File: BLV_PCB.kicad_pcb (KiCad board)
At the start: 4 copper layers, 89.7 x 89.7 mm, 88 parts, among them J1 Cube0 JST-PH, J2 Cube0 JST-PH, J3 Cube0 JST-PH, J4 Micro_SD_Card, J5 Dupont Debug Headers, J6 USB_C_USB2.0_16P, J8 USB_C_USB2.0_16P, Q1 Si2301CDS, SW1 SW_Push, SW2 SW_Push, SW5 SW_Push, U1 W25Q128JVS, U2 RP2350_60QFN, U3 TP4056, U4 AMS1117-3.3, U5 TPS61230DRCR, U6 NEO-M9N, U9 E22-400M33S, Y1 ABM8_262_T3

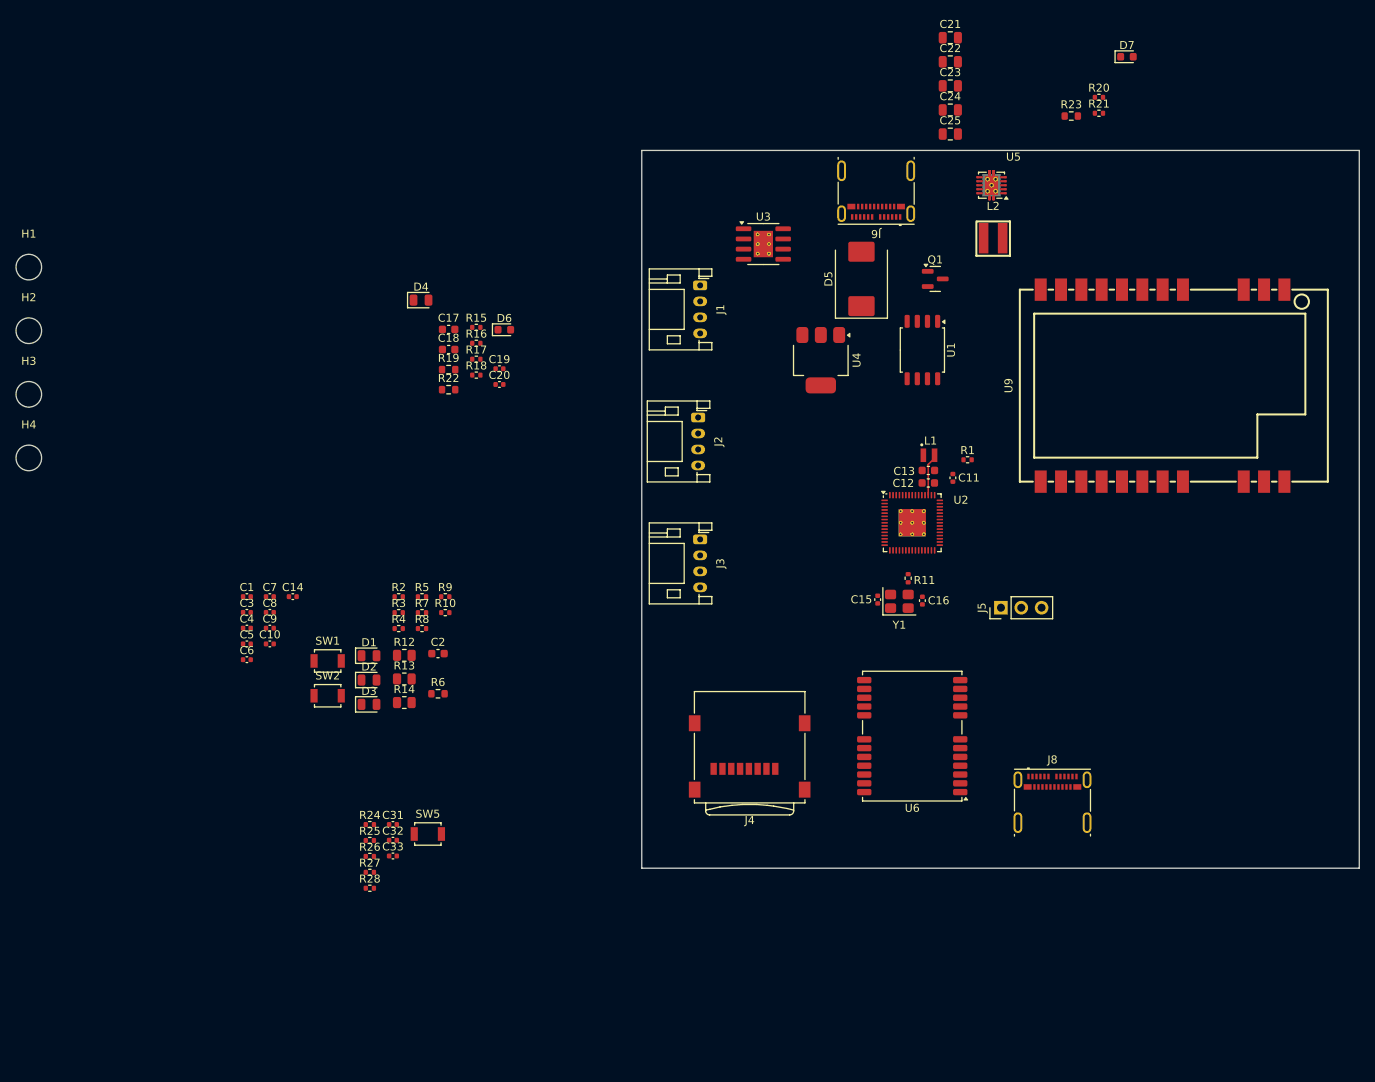
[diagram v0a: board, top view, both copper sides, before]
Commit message: Added footprints & routing 30%
- Added Dupont debug headers for UARTs.
- Added footprints: 18650 battery, E32-400M30S.
- Remove Battery Charger due to reliability issue.
- Routing 5V SMPS, 3V3 Regulator, Battery Holder.
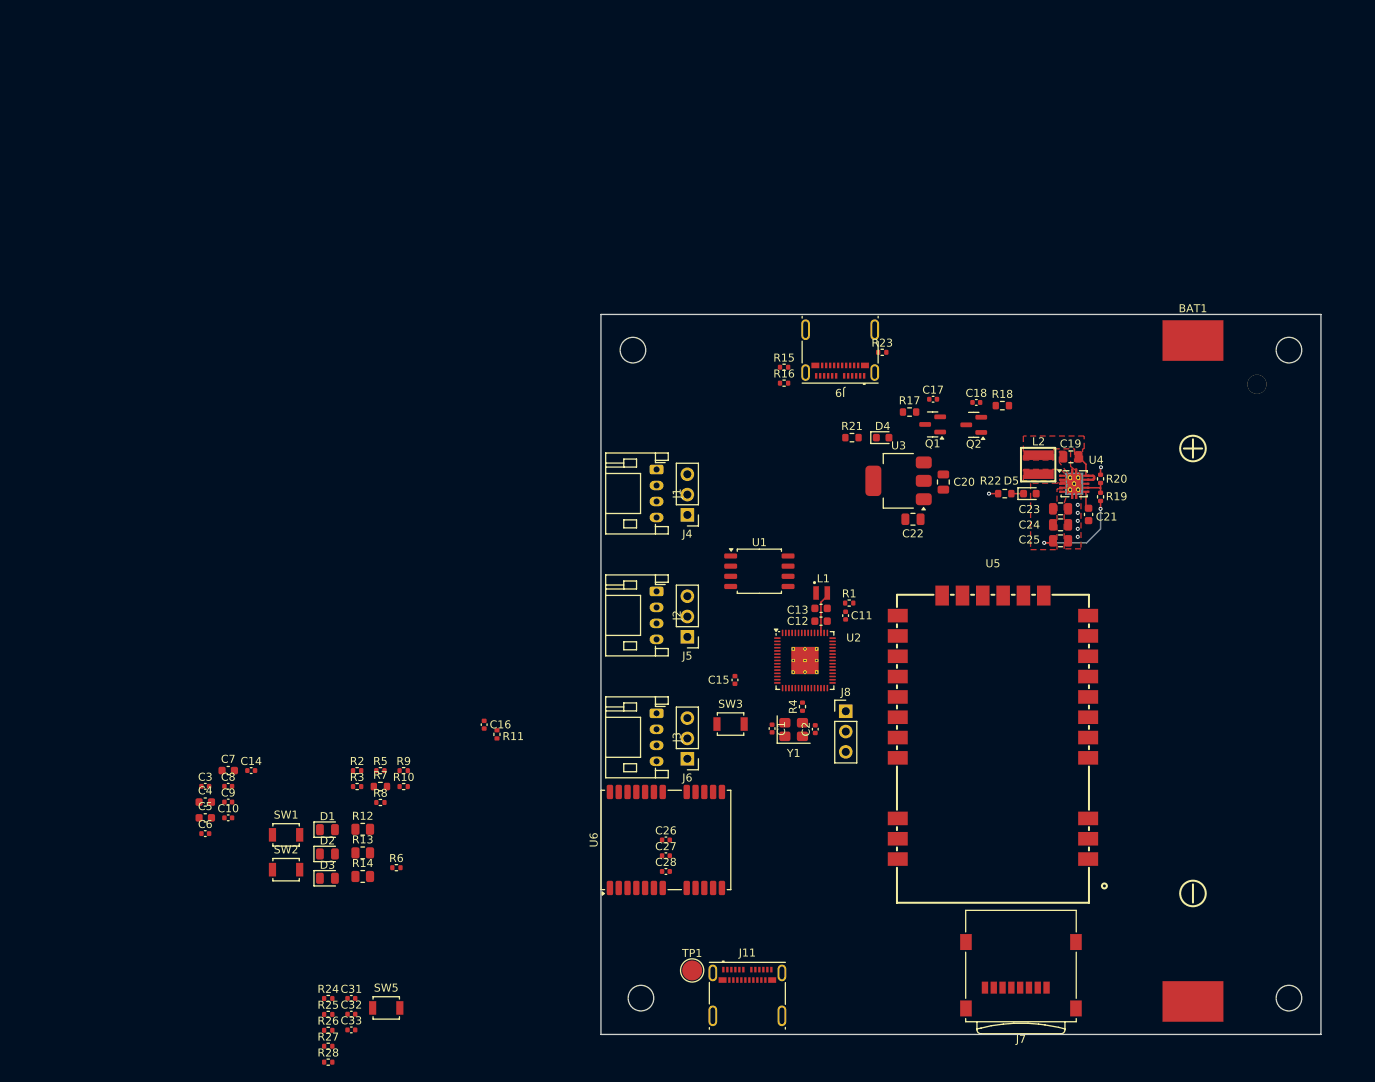
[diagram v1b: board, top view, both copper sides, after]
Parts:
- removed D6: YELLOW, LED_SMD:LED_0603_1608Metric
- removed D7: GREEN, LED_SMD:LED_0603_1608Metric
- removed U9: E22-400M33S, WIRELM-SMD_E22-400M30S:WIRELM-SMD_E22-400M33S
- added BAT1: BH-18650-B6AA002, easyeda2kicad:BATTERY-SMD_18650-1S-L77.1-W20.7-1, F.Cu at (204.0, 84.6)
- added C26: 10uF, Capacitor_SMD:C_0402_1005Metric, F.Cu at (138.1, 105.7)
- added C27: 1uF, Capacitor_SMD:C_0402_1005Metric, F.Cu at (138.1, 107.7)
- added C28: 100nF, Capacitor_SMD:C_0402_1005Metric, F.Cu at (138.1, 109.6)
- added J11: USB_C_USB2.0_16P, Connector_USB:USB_C_Receptacle_Molex_105450-0101, F.Cu at (148.3, 125.1)
- added J7: Micro_SD_Card, Connector_Card:microSD_HC_Wuerth_693072010801, F.Cu at (182.5, 122.6)
- added J9: USB_C_USB2.0_16P, Connector_USB:USB_C_Receptacle_Molex_105450-0101, F.Cu at (159.9, 44.5)
- added Q2: Si2301CDS, Package_TO_SOT_SMD:SOT-23, F.Cu at (176.6, 53.8)
- added SW3: SW_Push, Button_Switch_SMD:SW_SPST_B3U-1000P, F.Cu at (146.2, 91.2)
- added TP1: TestPoint, TestPoint:TestPoint_Pad_D2.5mm, F.Cu at (141.4, 122.0)
- C1: value 100n -> 15p
- C11, C12, C13: value 4u7 -> 100n
- C15, C16: value 15p -> 100n
- C17, C18: value 10u -> 100n; footprint Capacitor_SMD:C_0603_1608Metric -> Capacitor_SMD:C_0402_1005Metric
- C19: value 10u -> 22u; footprint Capacitor_SMD:C_0402_1005Metric -> Capacitor_SMD:C_0805_2012Metric
- C2: value 4u7 -> 15p; footprint Capacitor_SMD:C_0603_1608Metric -> Capacitor_SMD:C_0402_1005Metric
- C20: footprint Capacitor_SMD:C_0402_1005Metric -> Capacitor_SMD:C_0805_2012Metric
- C21: value 22u -> 10u; footprint Capacitor_SMD:C_0805_2012Metric -> Capacitor_SMD:C_0603_1608Metric
- C4, C5, C7: value 100n -> 4u7; footprint Capacitor_SMD:C_0402_1005Metric -> Capacitor_SMD:C_0603_1608Metric
- C8: value 100n -> 4u7
- D4: footprint LED_SMD:LED_0805_2012Metric -> LED_SMD:LED_0603_1608Metric
- D5: value SS36-E3/57T -> GREEN; footprint Diode_SMD:D_SMC -> LED_SMD:LED_0603_1608Metric
- J1, J2, J3: value Cube0 JST-PH -> Cube0_UART_JST-PH
- J4: value Micro_SD_Card -> Cube0_UART_Debug; footprint Connector_Card:microSD_HC_Wuerth_693072010801 -> Connector_PinHeader_2.54mm:PinHeader_1x03_P2.54mm_Vertical
- J5: value Dupont Debug Headers -> Cube0_UART_Debug
- J6: value USB_C_USB2.0_16P -> Cube0_UART_Debug; footprint Connector_USB:USB_C_Receptacle_Molex_105450-0101 -> Connector_PinHeader_2.54mm:PinHeader_1x03_P2.54mm_Vertical
- J8: value USB_C_USB2.0_16P -> Dupont Debug Headers; footprint Connector_USB:USB_C_Receptacle_Molex_105450-0101 -> Connector_PinHeader_2.54mm:PinHeader_1x03_P2.54mm_Vertical
- R1: value 33 -> DNF
- R11: value 1k -> 10k
- R17: value 5K1 -> 100k; footprint Resistor_SMD:R_0402_1005Metric -> Resistor_SMD:R_0603_1608Metric
- R18: value 2k2 -> 100k; footprint Resistor_SMD:R_0402_1005Metric -> Resistor_SMD:R_0603_1608Metric
- R19: value 10k -> 200k; footprint Resistor_SMD:R_0603_1608Metric -> Resistor_SMD:R_0402_1005Metric
- R2: value 27 -> 0
- R20: value 200k -> 49k9
- R21: value 49k9 -> 2k2; footprint Resistor_SMD:R_0402_1005Metric -> Resistor_SMD:R_0603_1608Metric
- R23: value 2k2 -> 5k1; footprint Resistor_SMD:R_0603_1608Metric -> Resistor_SMD:R_0402_1005Metric
- R25: value 5k1 -> 10k
- R3: value 27 -> 10k
- R4: value 10k -> 1k
- R5: value DNF -> 10k
- R6: value 1k -> 33; footprint Resistor_SMD:R_0603_1608Metric -> Resistor_SMD:R_0402_1005Metric
- R7: value 0 -> 1k; footprint Resistor_SMD:R_0402_1005Metric -> Resistor_SMD:R_0603_1608Metric
- R8, R9: value 10k -> 27
- U3: value TP4056 -> AMS1117-3.3; footprint Package_SO:SOIC-8-1EP_3.9x4.9mm_P1.27mm_EP2.41x3.3mm_ThermalVias -> Package_TO_SOT_SMD:SOT-223-3_TabPin2
- U4: value AMS1117-3.3 -> TPS61230DRCR; footprint Package_TO_SOT_SMD:SOT-223-3_TabPin2 -> Package_SON:Texas_S-PVSON-N10_ThermalVias
- U5: value TPS61230DRCR -> E32-400M30S; footprint Package_SON:Texas_S-PVSON-N10_ThermalVias -> easyeda2kicad:WIRELM-SMD_E32-400M30S
- moved H3 174.7 mm to (216.0, 125.5)
- moved H2 157.5 mm to (216.0, 44.5)
- moved H4 102.1 mm to (135.0, 125.5)
- moved R19 83.0 mm to (192.4, 62.8), turned to 90 degrees
- moved H1 76.2 mm to (134.0, 44.5)
- moved J6 74.8 mm to (140.8, 95.5)
- moved C19 72.3 mm to (188.8, 57.8), turned to 180 degrees
- moved R22 70.7 mm to (180.5, 62.4)
- moved U5 67.8 mm to (179.0, 91.6), turned to 0 degrees
- moved C1 67.7 mm to (151.4, 91.8), turned to -90 degrees
- moved C18 66.3 mm to (176.9, 51.0)
- moved R18 65.9 mm to (180.2, 51.4)
- moved C21 62.0 mm to (190.9, 65.0), turned to -90 degrees
- moved C17 61.2 mm to (171.5, 50.6)
- moved D4 60.2 mm to (165.2, 55.4)
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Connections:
- C1 pad 1: +1V1 -> GND
- C1 pad 2: GND -> /MCU/XIN
- C11 pad 1: /MCU/VREG_AVDD -> +3V3
- C13 pad 1: +1V1 -> +3V3
- C15 pad 1: GND -> +3V3
- C15 pad 2: /MCU/XIN -> GND
- C16 pad 1: GND -> +3V3
- C16 pad 2: /MCU/XOUT_R -> GND
- C17 pad 2: GND -> /Power/Vin
- C18 pad 2: GND -> /Power/Vin
- C19 pad 1: Net-(D5-K) -> /Power/Vin
- C2 pad 1: +1V1 -> GND
- C2 pad 2: GND -> /MCU/XOUT_R
- C20 pad 1: +3V3 -> /Power/Vin
- C21 pad 1: Net-(D5-K) -> /Power/5V_SMPS_SS
- C22 pad 1: Net-(U5-SS) -> +3V3
- C3 pad 1: +1V1 -> +3V3
- C5 pad 1: +3V3 -> +1V1
- C6 pad 1: +3V3 -> +1V1
- C7 pad 1: +3V3 -> +1V1
- C8 pad 1: +3V3 -> /MCU/VREG_AVDD
- C9 pad 1: +3V3 -> +1V1
- D4 pad 1: /Power/CHRG_LED -> /Power/LED_3V3
- D4 pad 2: VBUS -> +3V3
- D5 pad 1: Net-(D5-K) -> /Power/LED_5V
- D5 pad 2: VBUS -> +5V
- J1 pad 1: /MCU/CUBE_UART0_TX -> /Cube0_UART_TX
- J1 pad 2: /MCU/CUBE_UART0_RX -> /Cube0_UART_RX
- J2 pad 1: /MCU/CUBE_UART1_TX -> /Cube1_UART_TX
- J2 pad 2: /MCU/CUBE_UART1_RX -> /Cube1_UART_RX
- J3 pad 1: /MCU/CUBE_UART2_TX -> /Cube2_UART_TX
- J3 pad 2: /MCU/CUBE_UART2_RX -> /Cube2_UART_RX
- J4 pad 1: unconnected-(J4-DAT2-Pad1) -> GND
- J4 pad 2: /GNSS/SPI_CS -> /Cube0_UART_RX
- J4 pad 3: /GNSS/SPI_MOSI -> /Cube0_UART_TX
- J5 pad 1: /MCU/SWCLK -> GND
- J5 pad 2: /MCU/SWD -> /Cube1_UART_RX
- J5 pad 3: GND -> /Cube1_UART_TX
- L2 pad 1: Net-(D5-K) -> /Power/Vin
- L2 pad 2: Net-(L2-Pad2) -> /Power/5V_SMPS_SW
- Q1 pad 1: VBUS -> /Power/Vin
- Q1 pad 2: Net-(D5-K) -> VBUS
- Q1 pad 3: +BATT -> /Power/Vin
- R1 pad 1: +3V3 -> unconnected-(R1-Pad1)
- R1 pad 2: /MCU/VREG_AVDD -> /MCU/FLASH_SS
- R10 pad 1: GND -> /MCU/BUS_I2C0_SDA
- R10 pad 2: Net-(R10-Pad2) -> +3V3
- R11 pad 1: /MCU/XOUT_R -> /MCU/BUS_I2C0_SCL
- R11 pad 2: /MCU/XOUT -> +3V3
- R17 pad 1: /Power/CHRG_LED -> /Power/Vin
- R17 pad 2: /Power/~{CHRG} -> GND
- R18 pad 1: /Power/PROG -> /Power/Vin
- R19 pad 1: VBUS -> +5V
- R19 pad 2: GND -> /Power/5V_SMPS_FB
- R2 pad 1: USB_D+ -> /MCU/QSPI_SS
- R2 pad 2: Net-(U2-USB_DP) -> /MCU/FLASH_SS
- R20 pad 1: +5V -> /Power/5V_SMPS_FB
- R20 pad 2: Net-(U5-FB) -> GND
- R21 pad 1: Net-(U5-FB) -> GND
- R21 pad 2: GND -> /Power/LED_3V3
- R22 pad 2: /Power/LED_3V3 -> /Power/LED_5V
- R23 pad 1: GND -> /GNSS/USB2_CC2
- R23 pad 2: /Power/LED_5V -> GND
- R24 pad 1: /GNSS/USB2_CC2 -> /GNSS/USB2_CC1
- R25 pad 1: /GNSS/USB2_CC1 -> GND
- R25 pad 2: GND -> Net-(R25-Pad2)
- R3 pad 1: USB_D- -> +3V3
- R3 pad 2: Net-(U2-USB_DM) -> /MCU/FLASH_SS
- R4 pad 1: +3V3 -> /MCU/XOUT_R
- R4 pad 2: /MCU/FLASH_SS -> /MCU/XOUT
- R5 pad 1: unconnected-(R5-Pad1) -> GND
- R5 pad 2: /MCU/FLASH_SS -> Net-(R5-Pad2)
- R6 pad 1: /MCU/~{USB_BOOT} -> +3V3
- R6 pad 2: /MCU/QSPI_SS -> /MCU/VREG_AVDD
- R7 pad 1: /MCU/QSPI_SS -> /MCU/~{USB_BOOT}
- R7 pad 2: /MCU/FLASH_SS -> /MCU/QSPI_SS
- R8 pad 1: /MCU/BUS_I2C0_SDA -> USB_D+
- R8 pad 2: +3V3 -> Net-(U2-USB_DP)
- R9 pad 1: /MCU/BUS_I2C0_SCL -> USB_D-
- R9 pad 2: +3V3 -> Net-(U2-USB_DM)
- SW2 pad 1: Net-(R10-Pad2) -> Net-(R5-Pad2)
- U2 pad 12: /MCU/CUBE_UART2_TX -> /Cube2_UART_TX
- U2 pad 13: /MCU/CUBE_UART2_RX -> /Cube2_UART_RX
- U2 pad 2: /MCU/CUBE_UART0_TX -> /Cube0_UART_TX
- U2 pad 3: /MCU/CUBE_UART0_RX -> /Cube0_UART_RX
- U2 pad 7: /MCU/CUBE_UART1_TX -> /Cube1_UART_TX
- U2 pad 8: /MCU/CUBE_UART1_RX -> /Cube1_UART_RX
- U3 pad 2: /Power/PROG -> +3V3
- U3 pad 3: GND -> /Power/Vin
- U4 pad 1: GND -> /Power/5V_SMPS_SW
- U4 pad 2: +3V3 -> /Power/5V_SMPS_SW
- U4 pad 3: Net-(D5-K) -> +5V
- U5 pad 1: Net-(L2-Pad2) -> GND
- U5 pad 10: Net-(D5-K) -> +5V
- U5 pad 2: Net-(L2-Pad2) -> GND
- U5 pad 3: +5V -> GND
- U5 pad 4: +5V -> GND
- U5 pad 5: unconnected-(U5-PG-Pad5)_1 -> GND
- U5 pad 6: Net-(U5-SS) -> unconnected-(U5-RXEN-Pad6)
- U5 pad 7: Net-(U5-FB) -> unconnected-(U5-TXEN-Pad7)
- U5 pad 9: Net-(D5-K) -> +5V
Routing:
- net +5V: track 0.00 -> 12.2 mm, vias 0 -> 2
- net /Power/Vin: track 0.00 -> 4.58 mm
- net /Power/5V_SMPS_FB: track 0.00 -> 2.55 mm
- net /Power/5V_SMPS_SS: track 0.00 -> 2.19 mm
- net GND: track 0.00 -> 2.11 mm, vias 0 -> 7
- net /Power/LED_5V: track 0.00 -> 1.52 mm
- added copper zone on F.Cu, net +5V
- added copper zone on F.Cu, net /Power/5V_SMPS_SW
- added copper zone on F.Cu, net /Power/Vin
- added copper zone on F.Cu, net GND
- added copper zone on In1.Cu, net GND
- added copper zone on In2.Cu, net GND
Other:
- board size 89.7 x 89.7 mm -> 90 x 90 mm

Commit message: Finished layout & DRC
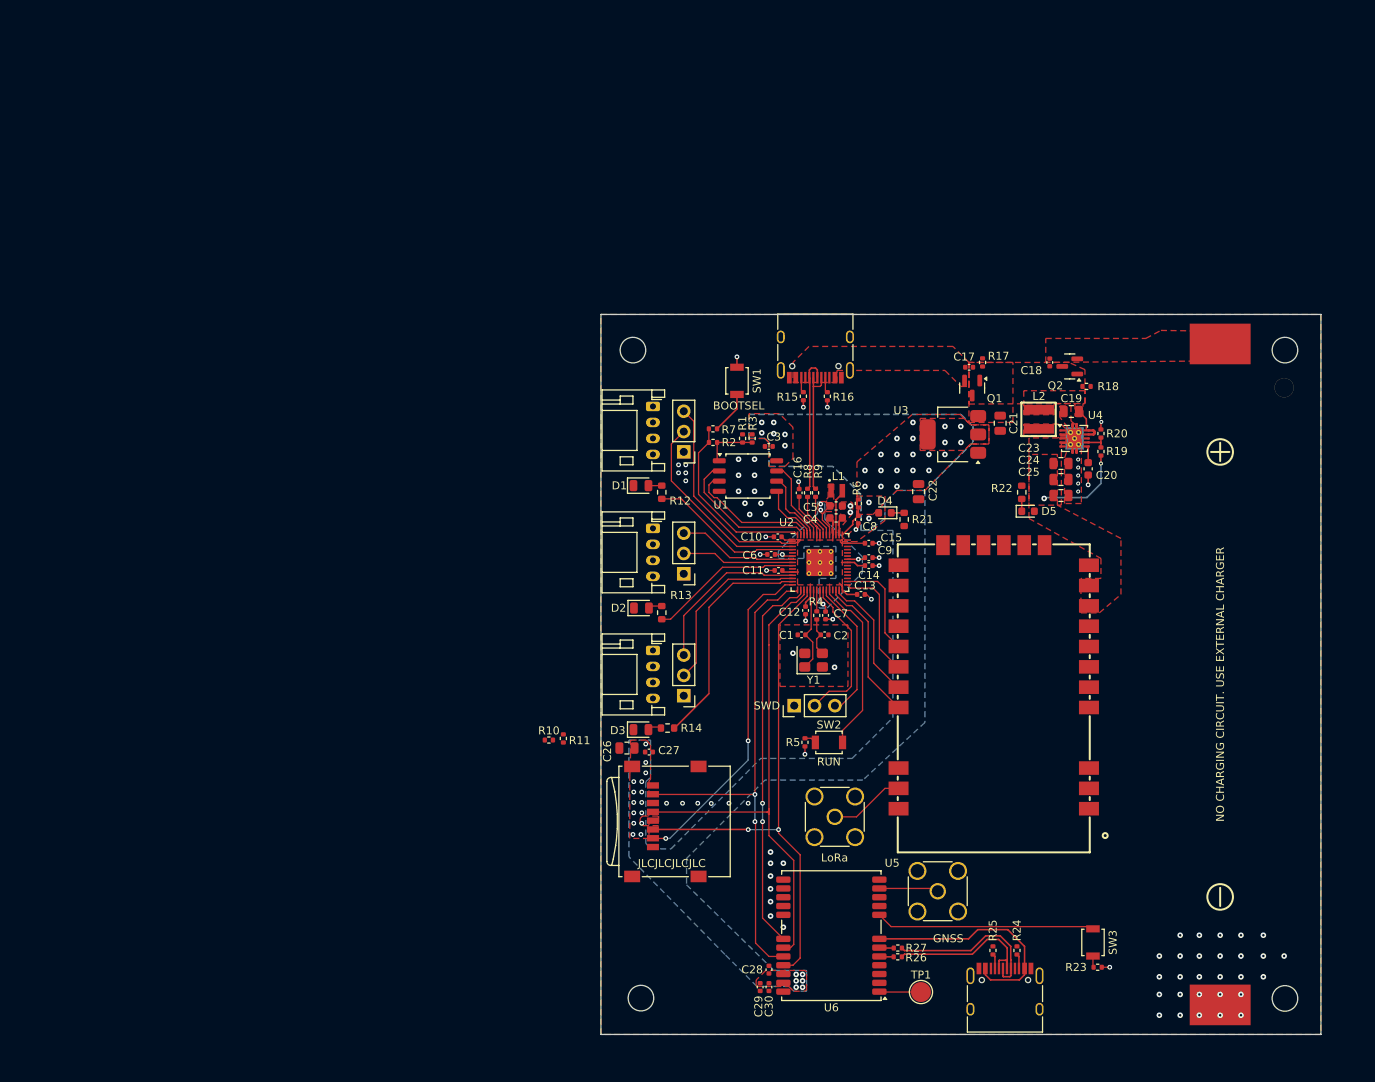
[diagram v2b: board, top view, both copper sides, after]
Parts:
- removed C31: 100nF, Capacitor_SMD:C_0402_1005Metric
- removed C32: 1uF, Capacitor_SMD:C_0402_1005Metric
- removed C33: 10uF, Capacitor_SMD:C_0402_1005Metric
- removed the J7 at (182.5, 122.6)
- removed R28: 10k, Resistor_SMD:R_0402_1005Metric
- removed SW5: SW_Push, Button_Switch_SMD:SW_SPST_B3U-1000P
- added C26: 22u, Capacitor_SMD:C_0805_2012Metric, F.Cu at (133.2, 94.2)
- added C27: 100n, Capacitor_SMD:C_0402_1005Metric, F.Cu at (136.0, 94.7)
- added J11: Micro_SD_Card, Connector_Card:microSD_HC_Wuerth_693072010801, F.Cu at (138.1, 103.4)
- added J12: RF SMA, Connector_Coaxial:SMA_Amphenol_132134_Vertical, F.Cu at (172.1, 112.1)
- added J9: RF SMA, Connector_Coaxial:SMA_Amphenol_132134_Vertical, F.Cu at (159.2, 102.8)
- C12, C13, C7: footprint Capacitor_SMD:C_0603_1608Metric -> Capacitor_SMD:C_0402_1005Metric
- C20: footprint Capacitor_SMD:C_0805_2012Metric -> Capacitor_SMD:C_0603_1608Metric
- C21: footprint Capacitor_SMD:C_0603_1608Metric -> Capacitor_SMD:C_0805_2012Metric
- J10: renamed from J11; footprint Connector_USB:USB_C_Receptacle_Molex_105450-0101 -> Connector_USB:USB_C_Receptacle_HRO_TYPE-C-31-M-12
- J8: renamed from J9; footprint Connector_USB:USB_C_Receptacle_Molex_105450-0101 -> Connector_USB:USB_C_Receptacle_HRO_TYPE-C-31-M-12
- R12, R13, R14: footprint Resistor_SMD:R_0805_2012Metric -> Resistor_SMD:R_0603_1608Metric
- R17, R18, R7: footprint Resistor_SMD:R_0603_1608Metric -> Resistor_SMD:R_0402_1005Metric
- R23: value 5k1 -> 10k
- R25: value 10k -> 5k1
- SW2: value SW_Push -> SW_RUN
- U2: footprint Package_DFN_QFN:QFN-60-1EP_7x7mm_P0.4mm_EP3.4x3.4mm_ThermalVias -> RP2350_60QFN_minimal:RP2350-QFN-60-1EP_7x7_P0.4mm_EP3.4x3.4mm_ThermalVias
- moved C5 88.0 mm to (159.4, 63.9)
- moved C4 86.5 mm to (159.4, 65.4)
- moved R24 86.3 mm to (182.0, 119.5), turned to 90 degrees
- moved C9 85.7 mm to (163.5, 70.4)
- moved C8 85.5 mm to (162.2, 65.6), turned to -90 degrees
- moved R25 83.5 mm to (179.0, 119.5), turned to 90 degrees
- moved C3 82.3 mm to (151.0, 56.5), turned to 180 degrees
- moved R23 81.4 mm to (192.1, 121.6), turned to 180 degrees
- moved C14 81.3 mm to (163.5, 71.4)
- moved SW1 80.0 mm to (147.0, 48.3), turned to -90 degrees
- moved C6 78.9 mm to (151.3, 70.0), turned to 180 degrees
- moved C10 77.1 mm to (152.1, 67.8), turned to 180 degrees
- moved C7 77.1 mm to (158.1, 77.6), turned to -90 degrees
- moved R6 73.5 mm to (162.2, 63.6), turned to -90 degrees
- moved R27 72.3 mm to (167.1, 119.2), turned to 180 degrees
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- renumbered C26 to C28, C27 to C29, C28 to C30, J8 to J7
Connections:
- net /GNSS/SPI_CS renamed /GNSS & MicroSD/SPI_CS0
- net /GNSS/SPI_MISO renamed /GNSS & MicroSD/SPI_MISO
- net /GNSS/SPI_MOSI renamed /GNSS & MicroSD/SPI_MOSI
- net /GNSS/SPI_SCK renamed /GNSS & MicroSD/SPI_SCK
- net /GNSS/USB2_D+ renamed /GNSS & MicroSD/USB2_D+
- net /GNSS/USB2_D- renamed /GNSS & MicroSD/USB2_D-
- net /GNSS/USB2_DM renamed /GNSS & MicroSD/USB2_DM
- net /GNSS/USB2_DP renamed /GNSS & MicroSD/USB2_DP
- net /GNSS/VDD_USB renamed /GNSS & MicroSD/VDD_USB
- net /GNSS/nRESET renamed /GNSS & MicroSD/GNSS_RST
- net Net-(D1-A) renamed /MCU/Cube0_LED_R
- net Net-(D2-A) renamed /MCU/Cube1_LED_R
- net Net-(D3-A) renamed /MCU/Cube2_LED_R
- net Net-(R5-Pad2) renamed /MCU/SW_RUN_R
- net Net-(U2-GPIO10) renamed /MCU/Cube2_LED
- net Net-(U2-GPIO2) renamed /MCU/Cube0_LED
- net Net-(U2-GPIO6) renamed /MCU/Cube1_LED
- net Net-(U2-USB_DM) renamed /MCU/MCU_USB_DM
- net Net-(U2-USB_DP) renamed /MCU/MCU_USB_DP
- C20 pad 1: /Power/Vin -> /Power/5V_SMPS_SS
- C21 pad 1: /Power/5V_SMPS_SS -> /Power/Vin
- J10 pad A5: /GNSS/USB2_CC1 -> /GNSS & MicroSD/USB2_CC1
- J10 pad B5: /GNSS/USB2_CC2 -> /GNSS & MicroSD/USB2_CC2
- J7 pad 2: /MCU/SWD -> /MCU/SWCLK
- J7 pad 3: /MCU/SWCLK -> /MCU/SWD
- R23 pad 1: /GNSS/USB2_CC2 -> GND
- R23 pad 2: GND -> /GNSS & MicroSD/GNSS_RST_R
- R24 pad 1: /GNSS/USB2_CC1 -> /GNSS & MicroSD/USB2_CC2
- R25 pad 1: GND -> /GNSS & MicroSD/USB2_CC1
- R25 pad 2: Net-(R25-Pad2) -> GND
- SW3 pad 1: Net-(R25-Pad2) -> /GNSS & MicroSD/GNSS_RST_R
- U2 pad 15: unconnected-(U2-GPIO11-Pad15) -> /GNSS & MicroSD/SPI_CS1
- U6 pad 11: /GNSS/GNSS_ANT -> /GNSS & MicroSD/GNSS_ANT
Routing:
- net /GNSS & MicroSD/SPI_MOSI: track 0.00 -> 66.8 mm, vias 0 -> 2
- net /GNSS & MicroSD/SPI_MISO: track 0.00 -> 64.8 mm, vias 0 -> 2
- net /GNSS & MicroSD/SPI_SCK: track 0.00 -> 64.6 mm
- net +3V3: track 0.00 -> 49.9 mm, vias 0 -> 49
- net /GNSS & MicroSD/SPI_CS0: track 0.00 -> 47.8 mm, vias 0 -> 2
- net /GNSS & MicroSD/SPI_CS1: track 0.00 -> 41.6 mm, vias 0 -> 2
- net /GNSS & MicroSD/VDD_USB: track 0.00 -> 29.2 mm
- net /MCU/Cube2_LED: track 0.00 -> 28.7 mm
- net /GNSS & MicroSD/GNSS_RST: track 0.00 -> 27.4 mm
- net /Cube0_UART_TX: track 0.00 -> 25.9 mm
- net /Cube0_UART_RX: track 0.00 -> 25.3 mm
- net /MCU/QSPI_SS: track 0.00 -> 23.2 mm
- net /Cube2_UART_RX: track 0.00 -> 22.4 mm
- net /GNSS & MicroSD/USB2_D+: track 0.00 -> 21.2 mm
- net /Cube2_UART_TX: track 0.00 -> 20.9 mm
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- added copper zone on B.Cu, net +1V1
- added copper zone on F.Cu, net +1V1
- added copper zone on B.Cu, net +3V3
- added copper zone on F.Cu, net +3V3
- added copper zone on F.Cu, net +BATT
- added copper zone on F.Cu, net VBUS
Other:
- board text added: "BOOTSEL"
- board text added: "GNSS"
- board text added: "JLCJLCJLCJLC"
- board text added: "LoRa"
- board text added: "NO CHARGING CIRCUIT. USE EXTERNAL CHARGER"
- board text added: "RUN"
- board text added: "SWD"

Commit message: Finished layouts and DRC
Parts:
- removed R10, R11: 10k, Resistor_SMD:R_0402_1005Metric
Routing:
- net /Cube0_UART_RX: track 25.3 -> 29.7 mm
- net /Cube1_UART_RX: track 14.1 -> 18.4 mm
- net /Cube2_UART_RX: track 22.4 -> 26.7 mm
- net /Cube1_UART_TX: track 14.9 -> 19.0 mm
- net /Cube0_UART_TX: track 25.9 -> 30.0 mm
- net /Cube2_UART_TX: track 20.9 -> 24.9 mm
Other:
- board text added: "Cube0 LED"
- board text added: "Cube1 LED"
- board text added: "Cube2 LED"
- board text added: "Funded with hope and dreams"
- board text added: "Made by TRI DO BLV PCB v1"
